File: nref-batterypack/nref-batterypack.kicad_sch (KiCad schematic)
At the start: 48 parts, among them J1 C3+, J2 DBG, J3 PACK_CONN, J4 C4+, J5 C2+, J6 C1+, J7 C1-, SW1 Reset, U1 BQ76905, U2 TPS259482, U3 MSPM0L130xRGE

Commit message: WIP batterypack-top polishing
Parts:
- added J8: BACK_CONN, Connector_JST:JST_SHL_SM02B-SHLS-TF_1x02-1MP_P1.00mm_Horizontal, symbol Connector_Generic:Conn_01x02
- added TP1: BSL Invoke, TestPoint:TestPoint_Pad_1.5x1.5mm, symbol Connector:TestPoint
- J1: value C3+ -> C3-
- J6: value C1+ -> C1-
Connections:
- net BAT-: now also J6.1 (Pin_1)
- net BSL_INVOKE: now also TP1.1
- net C2+: now reaches J5.1 (Pin_1), R3.2
- net C2+: now also J1.1 (Pin_1)
- net C1+: now reaches R4.2
- net C1+: now also J8.1 (Pin_1); no longer J6.1 (Pin_1)
- net C3+: now reaches R2.2
- net C3+: now also J8.2 (Pin_2); no longer J1.1 (Pin_1)
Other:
- moved on the sheet: J1, J4, J6, J7

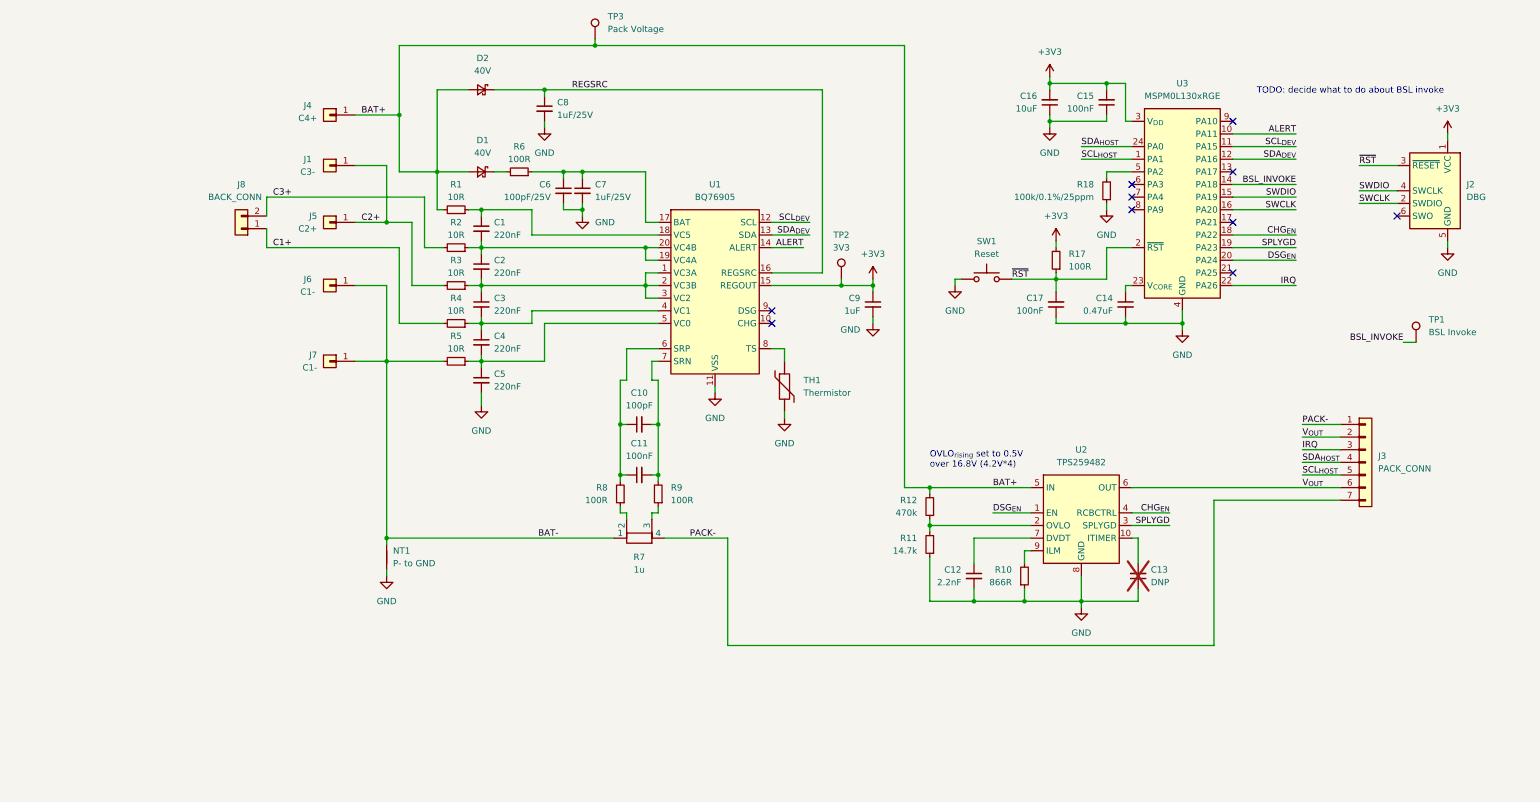
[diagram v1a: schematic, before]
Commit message: v2 of the bms now based on the final outline
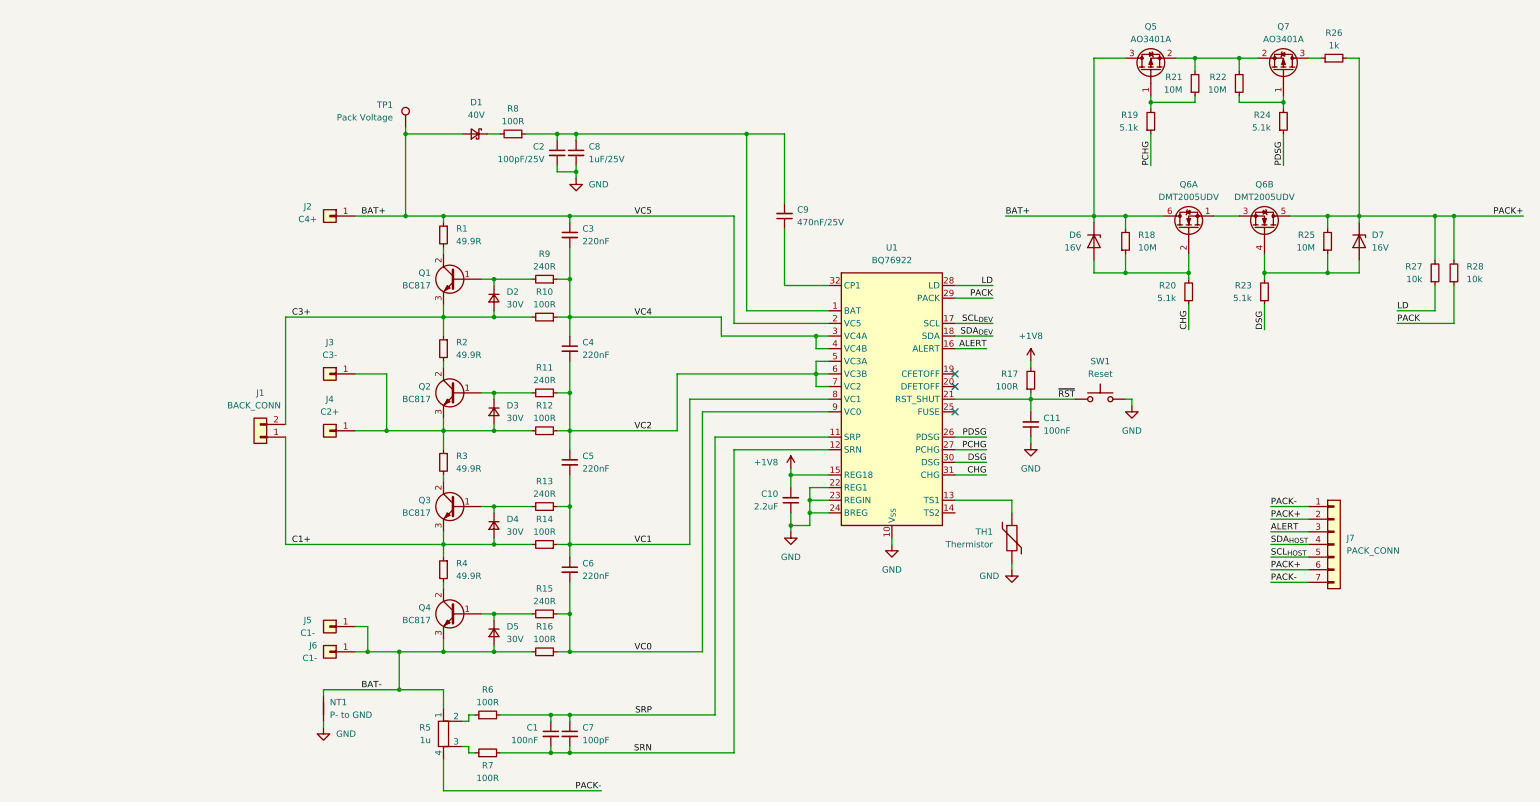
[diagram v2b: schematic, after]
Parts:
- removed C12: 2.2nF, Capacitor_SMD:C_0402_1005Metric, symbol Device:C_Small
- removed C13: DNP, Capacitor_SMD:C_0402_1005Metric, symbol Device:C_Small
- removed C14: 0.47uF, Capacitor_SMD:C_0402_1005Metric, symbol Device:C_Small
- removed C15, C17: 100nF, Capacitor_SMD:C_0402_1005Metric, symbol Device:C_Small
- removed C16: 10uF, Capacitor_SMD:C_0603_1608Metric, symbol Device:C_Small
- removed D2: 40V, Diode_SMD:D_SOD-323, symbol Device:D_Schottky_Small
- removed J2: DBG, Connector:Tag-Connect_TC2030-IDC-NL_2x03_P1.27mm_Vertical, symbol Connector:Conn_ARM_SWD_TagConnect_TC2030-NL
- removed R5: 10R, Resistor_SMD:R_1206_3216Metric, symbol Device:R_Small
- removed R7: 1u, Resistor_SMD:R_Shunt_Vishay_WSK2512_6332Metric_T1.19mm, symbol Device:R_Shunt
- removed TP2: 3V3, TestPoint:TestPoint_Pad_1.5x1.5mm, symbol Connector:TestPoint
- removed TP3: Pack Voltage, TestPoint:TestPoint_Pad_1.5x1.5mm, symbol Connector:TestPoint
- removed U1: BQ76905, Package_DFN_QFN:QFN-20-1EP_3.5x3.5mm_P0.5mm_EP2x2mm_ThermalVias, symbol meansOfCircuitDesign:BQ76905
- removed U2: TPS259482, Automated:PowerWCSP12_YWP_TEX, symbol meansOfCircuitDesign:TPS25948x
- removed U3: MSPM0L130xRGE, Package_DFN_QFN:VQFN-24-1EP_4x4mm_P0.5mm_EP2.5x2.5mm_ThermalVias, symbol meansOfCircuitDesign:MSPM0L130xRGE
- added D2, D3, D4, D5: 30V, Diode_SMD:D_SOD-323F, symbol Device:D_Small
- added D6, D7: 16V, Diode_SMD:D_SOD-323, symbol Device:D_Zener
- added Q1, Q2, Q3, Q4: BC817, Package_TO_SOT_SMD:SOT-23, symbol Device:Q_NPN_BCE
- added Q5, Q7: AO3401A, Package_TO_SOT_SMD:SOT-23, symbol Transistor_FET:AO3401A
- added Q6: DMT2005UDV, Automated:Diodes_PowerDI3333-8_UXC_3.3x3.3mm_P0.65mm, symbol Device:Q_Dual_NMOS_S1G1S2G2D2D1
- added R13, R15: 240R, Resistor_SMD:R_0402_1005Metric, symbol Device:R_Small
- added R14, R16, R7: 100R, Resistor_SMD:R_0402_1005Metric, symbol Device:R_Small
- added R19, R20, R23, R24: 5.1k, Resistor_SMD:R_0402_1005Metric, symbol Device:R_Small
- added R21, R22, R25: 10M, Resistor_SMD:R_0402_1005Metric, symbol Device:R_Small
- added R26: 1k, Resistor_SMD:R_1206_3216Metric, symbol Device:R_Small
- added R27, R28: 10k, Resistor_SMD:R_0402_1005Metric, symbol Device:R_Small
- added R5: 1u, Resistor_SMD:R_Shunt_Vishay_WSK2512_6332Metric_T1.19mm, symbol Device:R_Shunt
- added U1: BQ76922, Package_DFN_QFN:Texas_RSN_WQFN-32-1EP_4x4mm_P0.4mm_EP2.8x2.8mm, symbol meansOfCircuitDesign:BQ76922
- C1: value 220nF -> 100nF; footprint Capacitor_SMD:C_0603_1608Metric -> Capacitor_SMD:C_0402_1005Metric
- C10: value 100pF -> 2.2uF; footprint Capacitor_SMD:C_0603_1608Metric -> Capacitor_SMD:C_0402_1005Metric
- C11, C3, C4, C5: footprint Capacitor_SMD:C_0603_1608Metric -> Capacitor_SMD:C_0402_1005Metric
- C2: value 220nF -> 100pF/25V
- C6: value 100pF/25V -> 220nF; footprint Capacitor_SMD:C_0603_1608Metric -> Capacitor_SMD:C_0402_1005Metric
- C7: value 1uF/25V -> 100pF; footprint Capacitor_SMD:C_0603_1608Metric -> Capacitor_SMD:C_0402_1005Metric
- C9: value 1uF -> 470nF/25V; footprint Capacitor_SMD:C_0402_1005Metric -> Capacitor_SMD:C_0603_1608Metric
- R1, R2, R3, R4: value 10R -> 49.9R
- R10: value 866R -> 100R
- R11: value 14.7k -> 240R
- R12: value 470k -> 100R
- R17, R8: footprint Resistor_SMD:R_0603_1608Metric -> Resistor_SMD:R_0402_1005Metric
- R18: value 100k/0.1%/25ppm -> 10M
- R9: value 100R -> 240R; footprint Resistor_SMD:R_0603_1608Metric -> Resistor_SMD:R_0402_1005Metric
- TP1: value BSL Invoke -> Pack Voltage
- renumbered J8 to J1, J4 to J2, J1 to J3, J5 to J4, J6 to J5, J7 to J6, J3 to J7
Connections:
- net BSL_INVOKE is gone; now on net BAT+: TP1.1
- net IRQ is gone; now on net ALERT: J7.3 (Pin_3)
- net REGSRC is gone; now on an unnamed net: C8.1
- net ALERT: now also U1.16 (ALERT)
- net BAT-: now also D5.2 (A), Q4.3 (E), R16.2, R5.1
- net C1+: now also R4.1, D4.2 (A), Q3.3 (E), R14.2; no longer R4.2
- net C3+: now also R10.2, R2.1, D2.2 (A), Q1.3 (E); no longer R2.2
- net GND: now also C10.1, C11.1, C2.2, U1.10 (V_{SS}), U1.22 (REG1), U1.23 (REGIN), U1.24 (BREG), U1.33 (EP); no longer C5.2, C6.2, C7.2, C9.2, R10.1, R11.1, R18.1
- net PACK-: now also R5.4
- net SCL_{DEV}: now also U1.17 (SCL)
- net SDA_{DEV}: now also U1.18 (SDA)
- net ~{RST}: now also C11.2, U1.21 (RST_SHUT)
- net at R8.1: now also C2.1, C9.2, U1.1 (BAT)
- net VC2: now reaches C4.2, C5.1
- net VC2: now also R11.1, R12.1, U1.5 (VC3A), U1.6 (VC3B), U1.7 (VC2)
- net at R11.2: now also D3.1 (K), Q2.1 (B); no longer R12.1
- net VC4: now reaches R9.1
- net VC4: now also C3.2, C4.1, R10.1, U1.3 (VC4A), U1.4 (VC4B)
- net at D1.1 (K): now also R8.2; no longer R6.2
- net BAT+: now reaches R1.1
- net BAT+: now also C3.1, D1.2 (A), J2.1 (Pin_1), R18.2, D6.1 (K), Q5.3 (D), Q6.6 (D), U1.2 (VC5); no longer C1.1
- net at TH1.1: now also U1.13 (TS1)
- net +3V3: no longer names the net of C9.1
- net +3V3: now also U1.32 (CP1); no longer R17.2
- net C2+: no longer names the net of J3.1 (Pin_1), J4.1 (Pin_1)
- net C2+: now also R12.2, R3.1, D3.2 (A), Q2.3 (E); no longer R3.2
- removed net IN: D1.2 (A), J2.1 (Pin_1), R1.2, R12.2
- net V_{OUT} renamed PACK+
- net PACK+: now also D7.1 (K), Q6.5 (D), R25.2, R26.2, R27.2, R28.2
- new net: Q5.1 (G), R19.2, R21.1
- new net: Q5.2 (S), Q7.2 (S), R21.2, R22.2
- new net: D4.1 (K), Q3.1 (B), R13.2
- new net: Q3.2 (C), R3.2
- new net: Q7.3 (D), R26.1
- new net: D5.1 (K), Q4.1 (B), R15.2
- new net: Q7.1 (G), R22.1, R24.2
- new net: Q2.2 (C), R2.2
- new net: Q6.1 (S), Q6.3 (S)
- new net: D7.2 (A), Q6.4 (G), R23.2, R25.1
- new net: R5.2, R6.1
- new net: R5.3, R7.1
- new net: Q4.2 (C), R4.2
- new net: D2.1 (K), Q1.1 (B), R9.2
- new net: Q1.2 (C), R1.2
- new net: D6.2 (A), Q6.2 (G), R18.1, R20.2
- new net +1V8: C10.2, R17.2, U1.15 (REG18)
- new net CHG: R20.1, U1.31 (CHG)
- new net DSG: R23.1, U1.30 (DSG)
- new net LD: R27.1, U1.28 (LD)
- new net PACK: R28.1, U1.29 (PACK)
- new net PCHG: R19.1, U1.27 (PCHG)
- new net PDSG: R24.1, U1.26 (PDSG)
- new net SRN: C1.2, C7.2, R7.2, U1.12 (SRN)
- new net SRP: C1.1, C7.1, R6.2, U1.11 (SRP)
- new net VC0: C6.2, R15.1, R16.1, U1.9 (VC0)
- new net VC1: C5.2, C6.1, R13.1, R14.1, U1.8 (VC1)
- no-connect marks 10 -> 3
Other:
- note removed: "OVLO_{rising} set to 0.5V over 16.8V (4.2V*4)"
- note removed: "TODO: decide what to do about BSL invoke"
- moved on the sheet: J1, J2, J3, J4, J5, J6, J7

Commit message: batterypack: pick parts
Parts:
- C1, C11: MPN (none) -> GRM155R71C104KA88J; Manufacturer (none) -> Murata
- C10: MPN (none) -> GRM155R61E225ME15D; Manufacturer (none) -> Murata
- C2: MPN (none) -> GCM1885C2A101JA16D; Manufacturer (none) -> Murata
- C3, C4, C5, C6: MPN (none) -> GRT155C81E224KE01D; Manufacturer (none) -> Murata
- C7: MPN (none) -> GRM1555C1H101JA01D; Manufacturer (none) -> Murata
- C8: MPN (none) -> GRT188R61H105KE13D; Manufacturer (none) -> Murata
- C9: MPN (none) -> GRM188R71E474KA12D; Manufacturer (none) -> Murata
- D1: MPN (none) -> B140WS-7; Manufacturer (none) -> Diodes
- D2, D3, D4, D5: MPN (none) -> PMEG3015EJ,115; Manufacturer (none) -> Nexperia
- D6, D7: MPN (none) -> BZX384-B16,115; Manufacturer (none) -> Nexperia
- J1: MPN (none) -> SM02B-SHLS-TF(LF)(SN); Manufacturer (none) -> JST
- J2, J3, J4, J5: MPN (none) -> S7131-45R; Manufacturer (none) -> Harwin
- J6, NT1, TP1: MPN (none) -> DNP; Manufacturer (none) -> DNP
- J7: MPN (none) -> SM07B-SHLS-TF(LF)(SN); Manufacturer (none) -> JST
- Q1, Q2, Q3, Q4: MPN (none) -> BC817-25LT1G; Manufacturer (none) -> onsemi
- Q5, Q7: MPN (none) -> AO3401A; Manufacturer (none) -> Alpha & Omega
- Q6: MPN (none) -> DMT3020LDV-7 (alternative); Manufacturer (none) -> Diodes
- R1, R2, R3, R4: MPN (none) -> RC1206FR-0749R9L; Manufacturer (none) -> Yageo
- R10, R12, R14, R16, R17, R6, R7, R8: MPN (none) -> RC0402FR-07100RL; Manufacturer (none) -> Yageo
- R11, R13, R15, R9: MPN (none) -> RC0402FR-07240RL; Manufacturer (none) -> Yageo
- R18, R21, R22, R25: MPN (none) -> RC0402FR-0710ML; Manufacturer (none) -> Yageo
- R19, R20, R23, R24: MPN (none) -> RC0402FR-075K1L; Manufacturer (none) -> Yageo
- R26: MPN (none) -> RC0402JR-071KL; Manufacturer (none) -> Yageo
- R27, R28: MPN (none) -> RC0402JR-0710KL; Manufacturer (none) -> Yageo
- R5: MPN (none) -> WSK25121L000FEA; Manufacturer (none) -> Vishay Dale
- SW1: MPN (none) -> PTS810 SJK 250 SMTR LFS; Manufacturer (none) -> C&K
- TH1: MPN (none) -> NTCGS163JX103DT7; Manufacturer (none) -> TDK
- U1: MPN (none) -> BQ76922; Manufacturer (none) -> TI

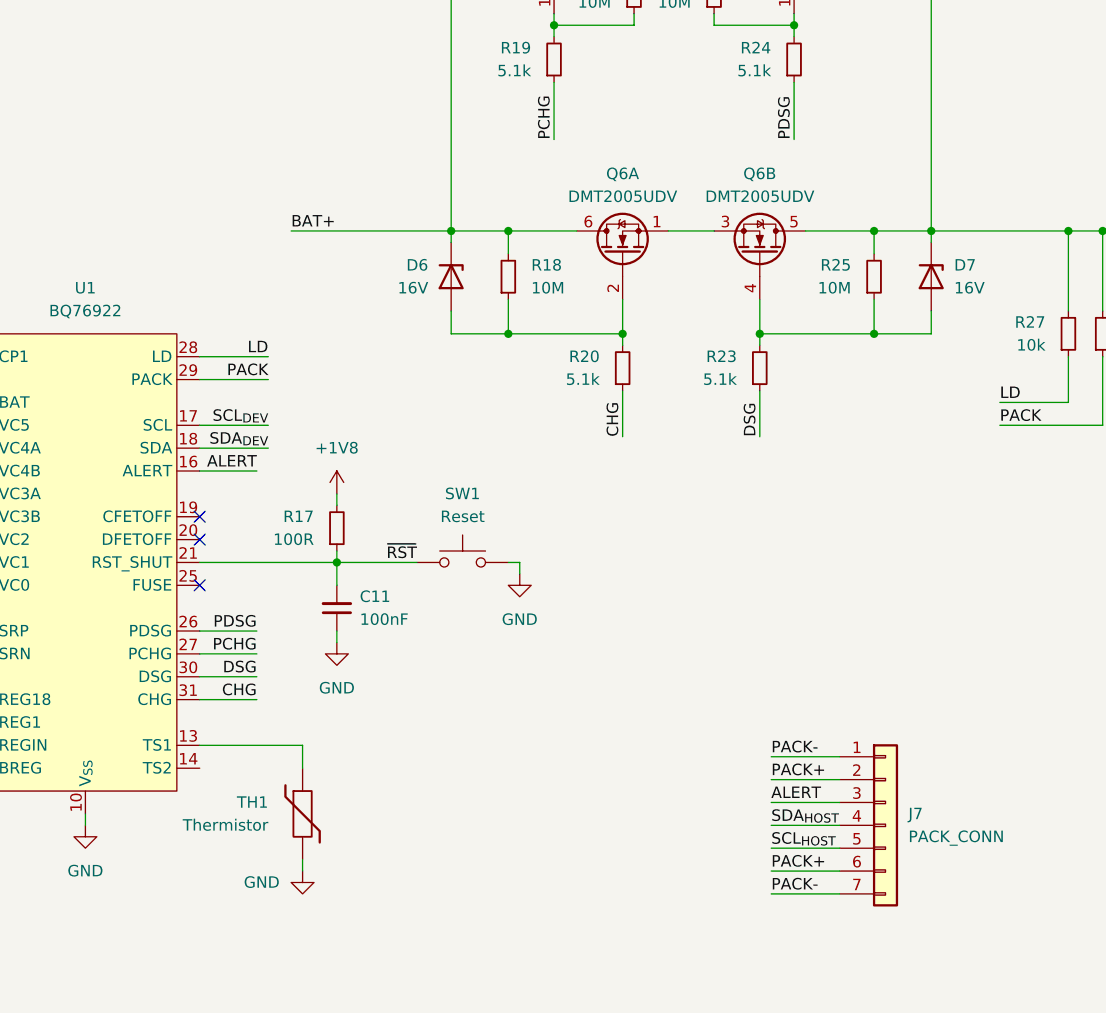
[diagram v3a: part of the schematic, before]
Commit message: fix load switch nmos and gate prot diode polarity
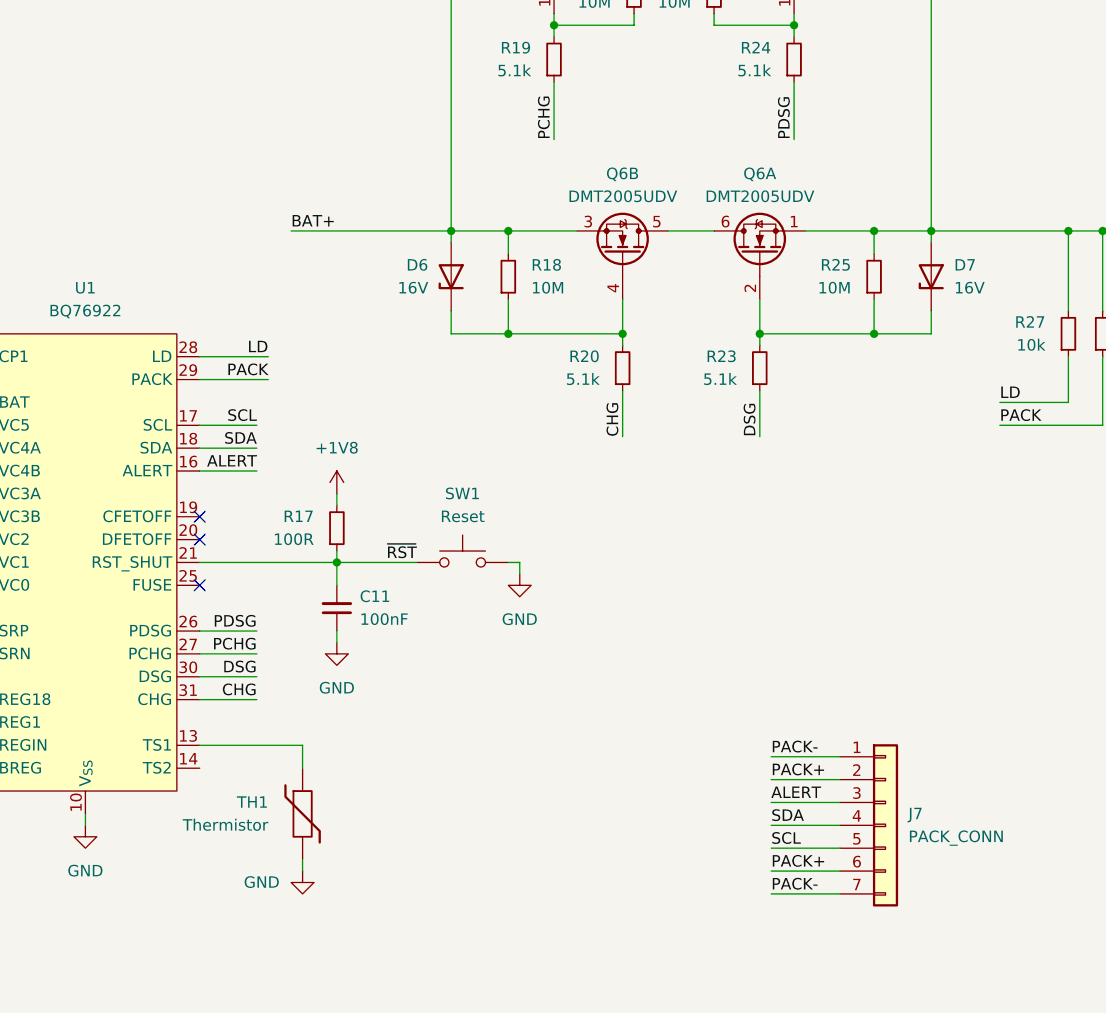
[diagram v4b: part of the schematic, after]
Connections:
- net SCL_{HOST} is gone; now on net SCL: J7.5 (Pin_5)
- net SDA_{HOST} is gone; now on net SDA: J7.4 (Pin_4)
- net BAT+: now also D6.2 (A), Q6.3 (S); no longer D6.1 (K), Q6.6 (D)
- net PACK+: now also D7.2 (A), Q6.1 (S); no longer D7.1 (K), Q6.5 (D)
- net at R23.2, R25.1: now also D7.1 (K), Q6.2 (G); no longer D7.2 (A), Q6.4 (G)
- net at R18.1, R20.2: now also D6.1 (K), Q6.4 (G); no longer D6.2 (A), Q6.2 (G)
- net SCL_{DEV} renamed SCL
- net SDA_{DEV} renamed SDA
- new net: Q6.5 (D), Q6.6 (D)
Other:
- moved on the sheet: D6, D7, Q6A, Q6B
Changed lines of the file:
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@@
 	(wire
 		(pts
-			(xy 162.56 85.09) (xy 170.18 85.09)
+			(xy 162.56 85.09) (xy 168.91 85.09)
 		)
 		(stroke
@@
 	(wire
 		(pts
-			(xy 162.56 87.63) (xy 170.18 87.63)
+			(xy 162.56 87.63) (xy 168.91 87.63)
 		)
 		(stroke
@@
 		)
 	)
-	(label "SDA_{HOST}"
+	(label "SDA"
 		(at 226.06 129.54 0)
 		(fields_autoplaced yes)
@@
 		)
 	)
-	(label "SCL_{HOST}"
+	(label "SCL"
 		(at 226.06 132.08 0)
 		(fields_autoplaced yes)
@@
 		)
 	)
-	(label "SCL_{DEV}"
-		(at 170.18 85.09 180)
+	(label "SCL"
+		(at 168.91 85.09 180)
 		(fields_autoplaced yes)
 		(effects
@@
 		)
 	)
-	(label "SDA_{DEV}"
-		(at 170.18 87.63 180)
+	(label "SDA"
+		(at 168.91 87.63 180)
 		(fields_autoplaced yes)
 		(effects
@@
 	(symbol
 		(lib_id "Device:Q_Dual_NMOS_S1G1S2G2D2D1")
-		(at 224.79 66.04 270)
+		(at 209.55 66.04 270)
 		(mirror x)
 		(unit 2)
@@
 		(fields_autoplaced yes)
 		(property "Reference" "Q6"
-			(at 224.79 57.15 90)
+			(at 209.55 57.15 90)
 			(effects
 				(font
@@
 		)
 		(property "Value" "DMT2005UDV"
-			(at 224.79 59.69 90)
+			(at 209.55 59.69 90)
 			(effects
 				(font
@@
 		)
 		(property "Footprint" "Automated:Diodes_PowerDI3333-8_UXC_3.3x3.3mm_P0.65mm"
-			(at 224.79 60.96 0)
+			(at 209.55 60.96 0)
 			(effects
 				(font
@@
 		)
 		(property "Datasheet" "~"
-			(at 224.79 60.96 0)
+			(at 209.55 60.96 0)
 			(effects
 				(font
@@
 		)
 		(property "Description" "Dual NMOS transistor, 6 pin package"
-			(at 212.598 63.754 0)
+			(at 197.358 63.754 0)
 			(effects
 				(font
@@
 		)
 		(property "MPN" "DMT3020LDV-7 (alternative)"
-			(at 224.79 66.04 0)
+			(at 209.55 66.04 0)
 			(effects
 				(font
@@
 		)
 		(property "Manufacturer" "Diodes"
-			(at 224.79 66.04 0)
+			(at 209.55 66.04 0)
 			(effects
 				(font
@@
 	(symbol
 		(lib_id "Device:D_Zener")
-		(at 190.5 68.58 270)
+		(at 190.5 68.58 90)
 		(unit 1)
 		(exclude_from_sim no)
@@
 					(size 1.27 1.27)
 				)
-				(justify right)
+				(justify left)
 			)
 		)
@@
 					(size 1.27 1.27)
 				)
-				(justify right)
+				(justify left)
 			)
 		)
@@
 	(symbol
 		(lib_id "Device:Q_Dual_NMOS_S1G1D2S2G2D1")
-		(at 209.55 66.04 90)
+		(at 224.79 66.04 90)
 		(unit 1)
 		(exclude_from_sim no)
@@
 		(fields_autoplaced yes)
 		(property "Reference" "Q6"
-			(at 209.55 57.15 90)
+			(at 224.79 57.15 90)
 			(effects
 				(font
@@
 		)
 		(property "Value" "DMT2005UDV"
-			(at 209.55 59.69 90)
+			(at 224.79 59.69 90)
 			(effects
 				(font
@@
 		)
 		(property "Footprint" "Automated:Diodes_PowerDI3333-8_UXC_3.3x3.3mm_P0.65mm"
-			(at 209.55 60.96 0)
+			(at 224.79 60.96 0)
 			(effects
 				(font
@@
 		)
 		(property "Datasheet" "https://www.diodes.com/assets/Datasheets/DMT2005UDV.pdf"
-			(at 209.55 60.96 0)
+			(at 224.79 60.96 0)
 			(effects
 				(font
@@
 		)
 		(property "Description" "Dual NMOS transistor, 6 pin package"
-			(at 209.55 66.04 0)
+			(at 224.79 66.04 0)
 			(effects
 				(font
@@
 		)
 		(property "MPN" "DMT3020LDV-7 (alternative)"
-			(at 209.55 66.04 0)
+			(at 224.79 66.04 0)
 			(effects
 				(font
@@
 		)
 		(property "Manufacturer" "Diodes"
-			(at 209.55 66.04 0)
+			(at 224.79 66.04 0)
 			(effects
 				(font
@@
 	(symbol
 		(lib_id "Device:D_Zener")
-		(at 243.84 68.58 270)
+		(at 243.84 68.58 90)
 		(unit 1)
 		(exclude_from_sim no)
@@
 					(size 1.27 1.27)
 				)
-				(justify left)
+				(justify right)
 			)
 		)
@@
 					(size 1.27 1.27)
 				)
-				(justify left)
+				(justify right)
 			)
 		)
